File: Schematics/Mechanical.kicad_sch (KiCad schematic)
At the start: 12 parts

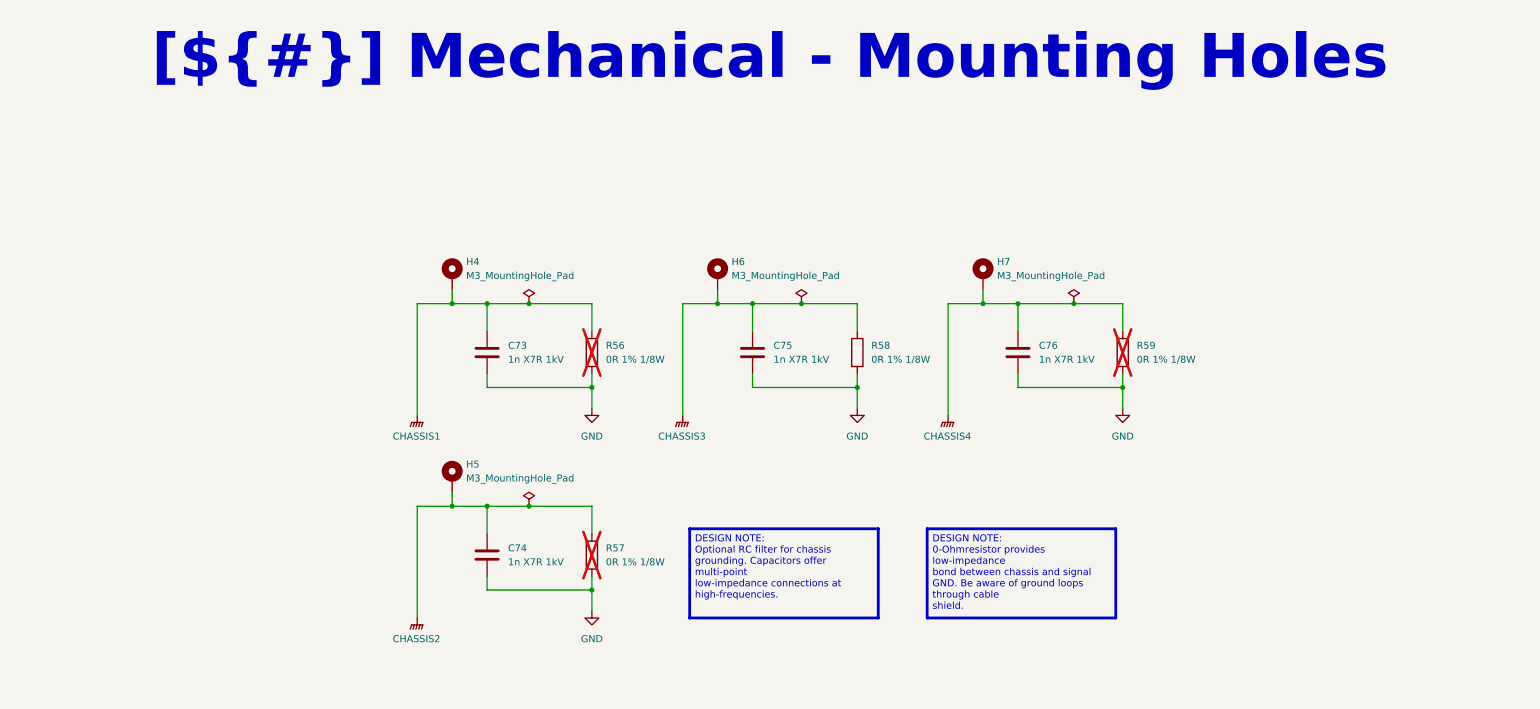
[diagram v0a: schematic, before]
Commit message: Clean up schematic design notes; export schematic and PCB artwork PDFs
- Remove firmware-only notes (boot sequence, calibration procedure,
  firmware SPI/PWM settings) and template/empty text; keep hardware facts
- Tighten wording of all DESIGN/SPEC/ASSEMBLY/REV 1 notes and resize
  boxes so no note text wraps or overflows
- Re-export schematic PDF
- Add PCB artwork PDFs (combined and one per layer: silk, paste, mask,
  L1-L6 copper), board outline on every page

Co-Authored-By: Claude Opus 5.5 <noreply@anthropic.com>
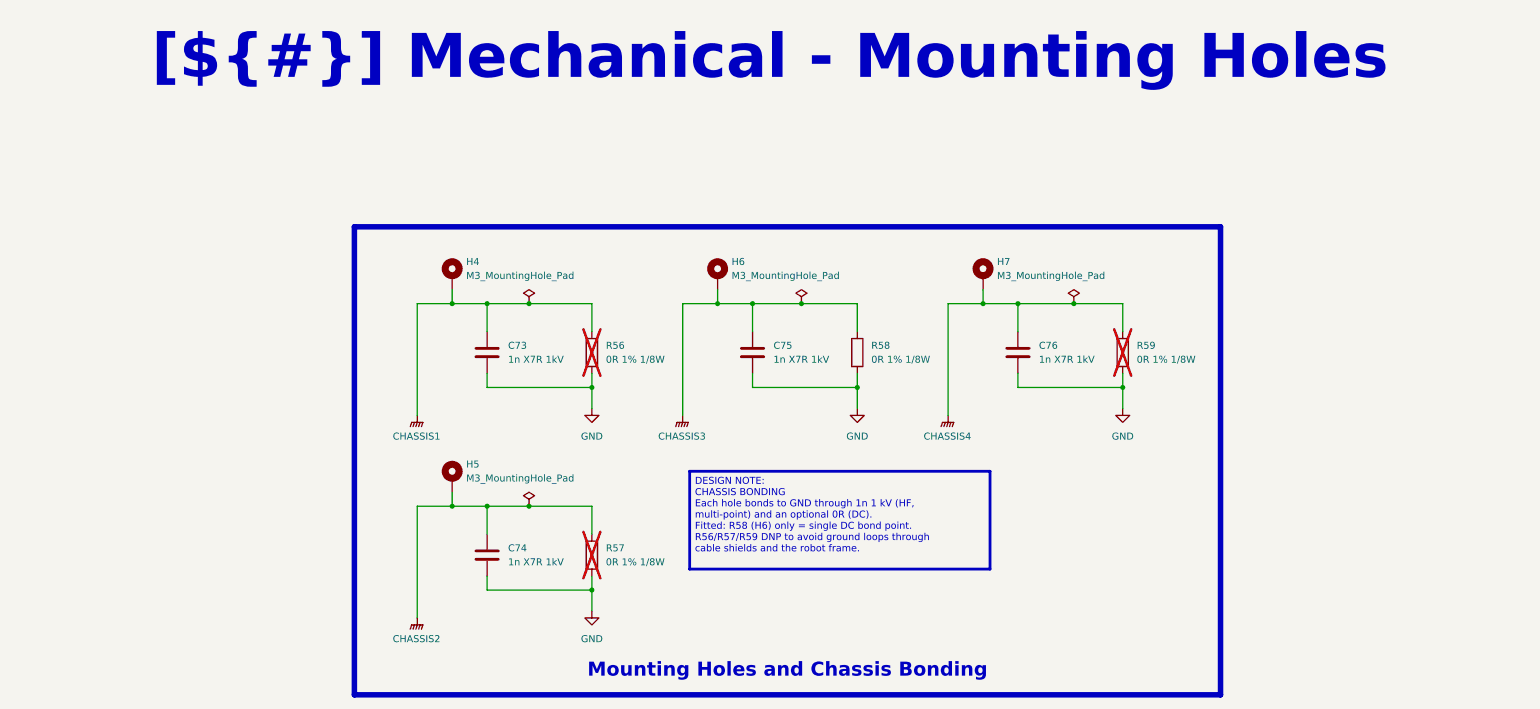
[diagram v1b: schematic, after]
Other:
- company: (none) -> ${COMPANY}
- title: (none) -> Mechanical - Mounting
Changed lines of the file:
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@@
 	(generator_version "10.0")
 	(paper "A4")
-	(text ""
-		(exclude_from_sim no)
-		(at 174.498 113.0301 0)
-		(effects
-			(font
-				(size 1.27 1.27)
-			)
-		)
+	(title_block
+		(title "Mechanical - Mounting")
+		(date "${RELEASE_DATE}")
+		(rev "${REVISION}")
+		(company "${COMPANY}")
 	)
 	(text_box "[${#}] Mechanical - Mounting Holes"
@@
 		)
 	)
-	(text_box "DESIGN NOTE: \n0-Ohmresistor provides low-impedance\nbond between chassis and signal GND. Be aware of ground loops through cable\nshield."
-		(exclude_from_sim no)
-		(at 177.8 109.5139 0)
-		(size 34.29 16.2161)
-		(margins 0.9525 0.9525 0.9525 0.9525)
-		(stroke
-			(width 0.508)
-			(type solid)
-			(color 0 0 255 1)
-		)
-		(fill
-			(type color)
-			(color 255 255 255 1)
-		)
-		(effects
-			(font
-				(size 1.27 1.27)
-				(color 0 0 0 1)
-			)
-			(justify left top)
-		)
-	)
-	(text_box "DESIGN NOTE: \nOptional RC filter for chassis grounding. Capacitors offer multi-point\nlow-impedance connections at high-frequencies."
-		(exclude_from_sim no)
-		(at 134.62 109.514 0)
-		(size 34.29 16.216)
-		(margins 0.9525 0.9525 0.9525 0.9525)
-		(stroke
-			(width 0.508)
-			(type solid)
-			(color 0 0 255 1)
-		)
-		(fill
-			(type color)
-			(color 255 255 255 1)
-		)
-		(effects
-			(font
-				(size 1.27 1.27)
-				(color 0 0 0 1)
-			)
-			(justify left top)
-		)
-	)
 	(junction
 		(at 97.79 68.58)
@@
 		)
 	)
-)
+	(rectangle
+		(start 73.66 54.61)
+		(end 231.14 139.7)
+		(stroke
+			(width 1)
+			(type default)
+			(color 200 200 200 1)
+		)
+		(fill
+			(type none)
+		)
+	)
+	(text_box "Mounting Holes and Chassis Bonding"
+		(exclude_from_sim no)
+		(at 73.66 130.6697 0)
+		(size 157.48 7.7603)
+		(margins 1.9049 1.9049 1.9049 1.9049)
+		(stroke
+			(width -0.0001)
+			(type solid)
+		)
+		(fill
+			(type none)
+		)
+		(effects
+			(font
+				(face "Times New Roman")
+				(size 2.54 2.54)
+				(thickness 0.508)
+				(bold yes)
+				(color 162 22 34 1)
+			)
+			(justify bottom)
+		)
+	)
+	(text_box "DESIGN NOTE:\nCHASSIS BONDING\nEach hole bonds to GND through 1n 1 kV (HF,\nmulti-point) and an optional 0R (DC).\nFitted: R58 (H6) only = single DC bond point.\nR56/R57/R59 DNP to avoid ground loops through\ncable shields and the robot frame."
+		(exclude_from_sim no)
+		(at 134.62 99.06 0)
+		(size 54.61 17.78)
+		(margins 0.9525 0.9525 0.9525 0.9525)
+		(stroke
+			(width 0.508)
+			(type solid)
+			(color 0 0 255 1)
+		)
+		(fill
+			(type color)
+			(color 255 255 255 1)
+		)
+		(effects
+			(font
+				(size 1.27 1.27)
+				(color 0 0 0 1)
+			)
+			(justify left top)
+		)
+	))
